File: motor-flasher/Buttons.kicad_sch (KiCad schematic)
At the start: 8 parts, among them U1 MAX16054AZT_T, U2 MAX16054AZT_T, U4 MAX16054AZT_T, U5 MAX16054AZT_T

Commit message: Beginning Layout Process
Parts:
- S11, S12, S13, S5: footprint revparts2:TS-1088-AR02016 -> Motor-Flasher:TS-1088-AR02016
- U1, U2, U4, U5: footprint revparts2:SOT95P275X110-6N -> Motor-Flasher:SOT95P275X110-6N
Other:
- moved on the sheet: S11, S12, S13, S5, U5

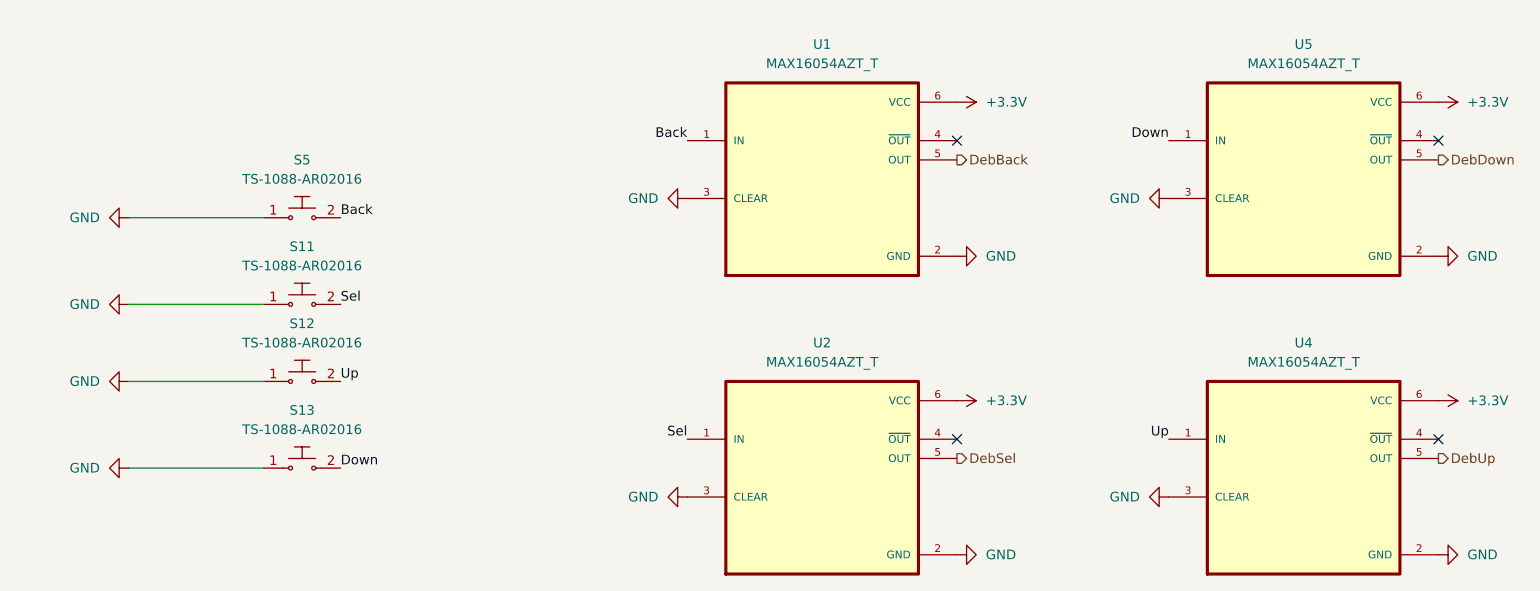
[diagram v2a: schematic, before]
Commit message: Removed ERC Errors and Warnings
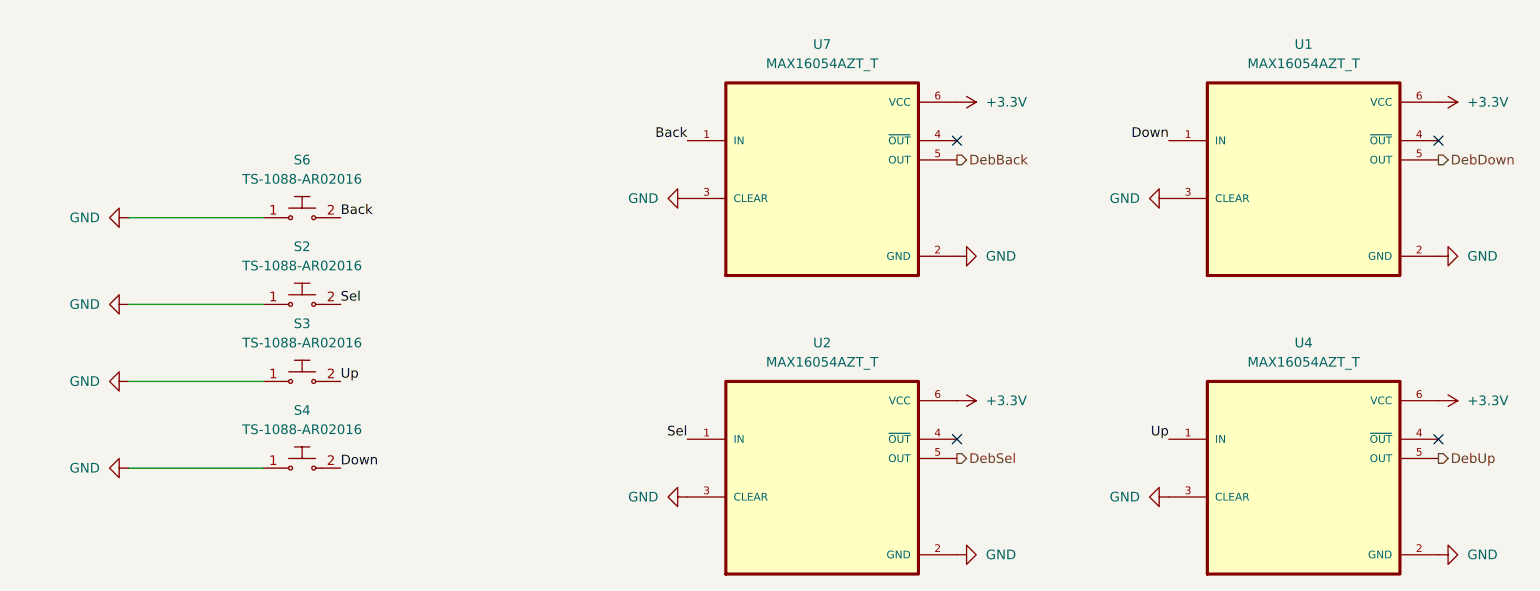
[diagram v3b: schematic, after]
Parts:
- removed S11, S12, S13, S5: TS-1088-AR02016, Motor-Flasher:TS-1088-AR02016, symbol dk_Pushbutton-Switches:GPTS203211B
- removed U1, U2, U4, U5: MAX16054AZT_T, Motor-Flasher:SOT95P275X110-6N, symbol MAX16054AZT_T:MAX16054AZT_T
- added S2, S3, S4, S6: TS-1088-AR02016, Motor-Flasher:TS-1088-AR02016, symbol Motor_Flasher_Modified:TS-1088-ARO2016_Mod
- added U1, U2, U4, U7: MAX16054AZT_T, Motor-Flasher:SOT95P275X110-6N, symbol Motor_Flasher_Modified:MAX16054AZT_T_Mod
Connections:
- net +3.3V: now also U1.6 (VCC), U2.6 (VCC), U4.6 (VCC), U7.6 (VCC)
- net Back: now also S6.2, U7.1 (IN)
- net DebBack: now also U7.5 (OUT)
- net DebDown: now also U1.5 (OUT)
- net DebSel: now also U2.5 (OUT)
- net DebUp: now also U4.5 (OUT)
- net Down: now also S4.2, U1.1 (IN)
- net GND: now also S2.1, S3.1, S4.1, S6.1, U1.2 (GND), U1.3 (CLEAR), U2.2 (GND), U2.3 (CLEAR), U4.2 (GND), U4.3 (CLEAR), U7.2 (GND), U7.3 (CLEAR)
- net Sel: now also S2.2, U2.1 (IN)
- net Up: now also S3.2, U4.1 (IN)
